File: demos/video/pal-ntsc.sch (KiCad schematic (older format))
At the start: 36 parts, among them U10 BT812, X2 30MHz

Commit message: Pcbnew: Minor fix in hotkeys. Demos: add an example to use  a local fp-lib-table and local libs, and update schematics and boards.
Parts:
- C1, C10, C11, C12, C13, C14, C15, C16, C2, C3, C4, C47, C5, C6, C65, C66, C7, C8, C9, R12, R14, R19, R2, R20, R25, R27, R3, R35: footprint (none) -> lib_smd:SM1206
- C62: footprint (none) -> lib_smd:SM1210L
- D1, D2, D3, D4: footprint (none) -> discret:D3
- L4: footprint (none) -> lib_smd:SM1812
- U10: footprint (none) -> lib_smd:PQFP160
- X2: footprint (none) -> discret:HC-18UV

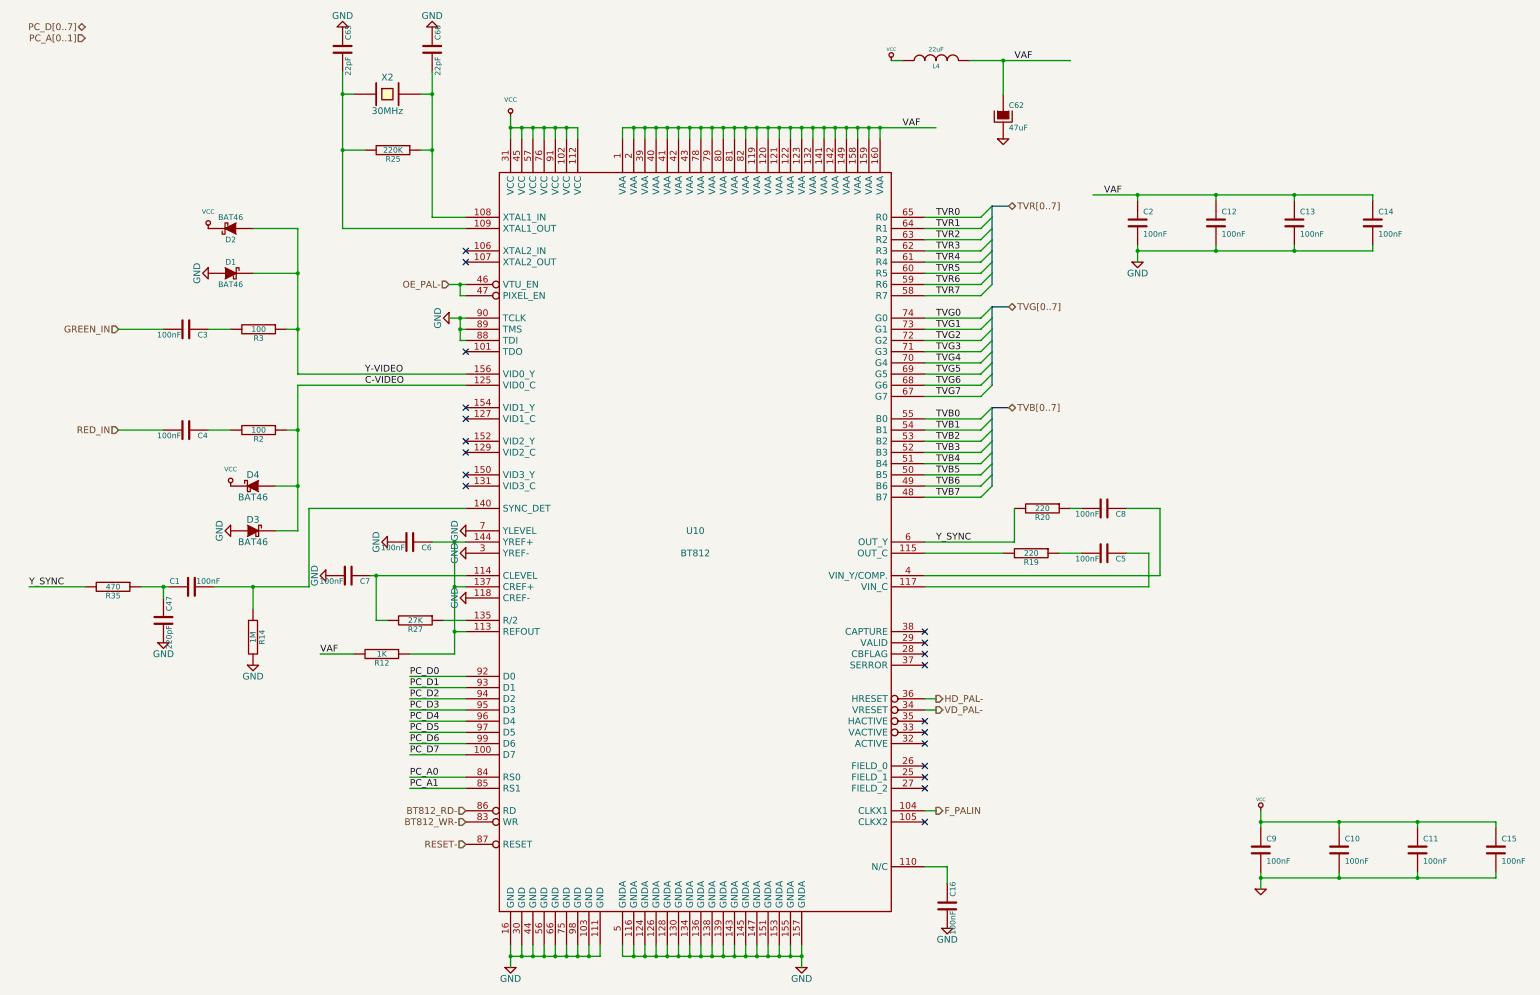
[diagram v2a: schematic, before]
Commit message: demos/ schematic tidying
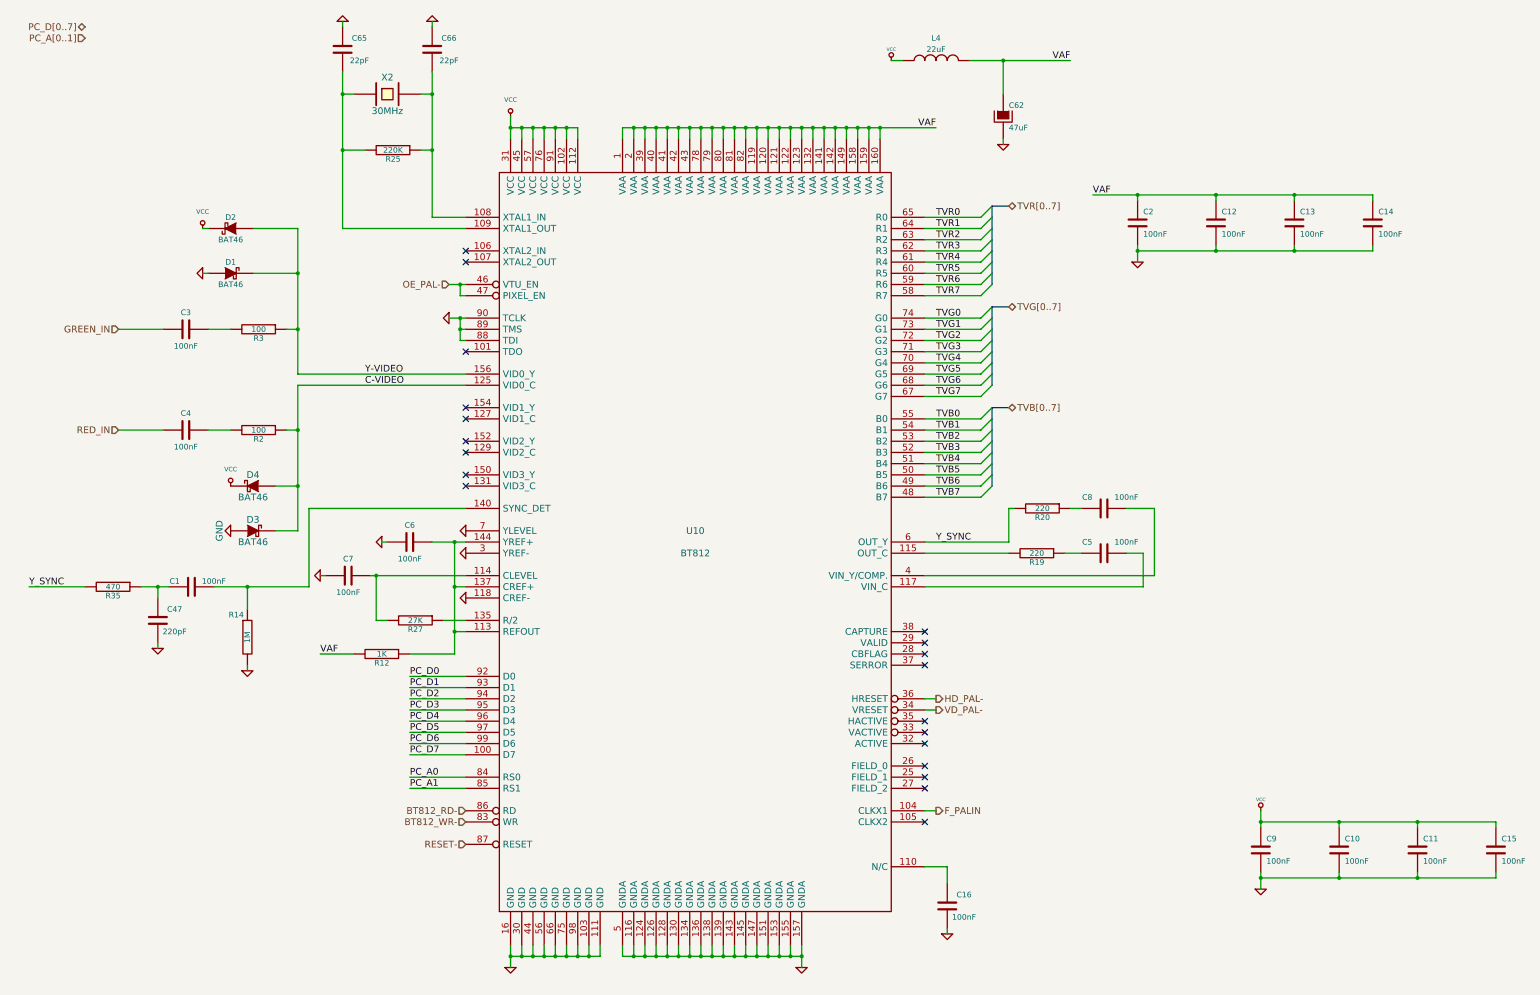
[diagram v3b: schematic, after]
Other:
- moved on the sheet: C47, R14, R19

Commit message: polygons in footprint body: fix incorrect calculation of polygons with clearance or outline thickness (fix bug #1511366) Clean demos
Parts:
- D1, D2, D3, D4: footprint discret:D3 -> Discret:D3
- X2: footprint discret:HC-18UV -> Discret:HC-18UV
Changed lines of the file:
@@
 EESchema Schematic File Version 2
+LIBS:video_schlib
 LIBS:power
-LIBS:device
-LIBS:transistors
-LIBS:conn
-LIBS:linear
-LIBS:regul
-LIBS:74xx
-LIBS:cmos4000
-LIBS:adc-dac
-LIBS:memory
-LIBS:xilinx
-LIBS:special
-LIBS:analog_switches
-LIBS:motorola
-LIBS:intel
-LIBS:audio
-LIBS:interface
-LIBS:philips
-LIBS:cypress
-LIBS:siliconi
 LIBS:video-cache
 EELAYER 25 0
@@
 F 0 "D1" H 3850 3800 50  0000 C CNN
 F 1 "BAT46" H 3850 3600 50  0000 C CNN
-F 2 "discret:D3" H 3850 3700 60  0001 C CNN
+F 2 "Discret:D3" H 3850 3700 60  0001 C CNN
 F 3 "" H 3850 3700 60  0001 C CNN
 	1    3850 3700
@@
 F 0 "D2" H 3850 3200 50  0000 C CNN
 F 1 "BAT46" H 3850 3400 50  0000 C CNN
-F 2 "discret:D3" H 3850 3300 60  0001 C CNN
+F 2 "Discret:D3" H 3850 3300 60  0001 C CNN
 F 3 "" H 3850 3300 60  0001 C CNN
 	1    3850 3300
@@
 F 0 "D3" H 4050 6100 60  0000 C CNN
 F 1 "BAT46" H 4050 5900 60  0000 C CNN
-F 2 "discret:D3" H 4050 6000 60  0001 C CNN
+F 2 "Discret:D3" H 4050 6000 60  0001 C CNN
 F 3 "" H 4050 6000 60  0001 C CNN
 	1    4050 6000
@@
 F 0 "D4" H 4050 5700 60  0000 C CNN
 F 1 "BAT46" H 4050 5500 60  0000 C CNN
-F 2 "discret:D3" H 4050 5600 60  0001 C CNN
+F 2 "Discret:D3" H 4050 5600 60  0001 C CNN
 F 3 "" H 4050 5600 60  0001 C CNN
 	1    4050 5600
@@
 F 0 "X2" H 5250 2250 60  0000 C CNN
 F 1 "30MHz" H 5250 1950 60  0000 C CNN
-F 2 "discret:HC-18UV" H 5250 2100 60  0001 C CNN
+F 2 "Discret:HC-18UV" H 5250 2100 60  0001 C CNN
 F 3 "" H 5250 2100 60  0001 C CNN
 	1    5250 2100
